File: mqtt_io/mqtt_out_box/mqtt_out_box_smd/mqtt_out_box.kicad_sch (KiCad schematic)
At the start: 59 parts, among them J1 Conn_01x04_Pin, J2 Conn_01x02, K1 FINDER-40.52, K2 FINDER-40.52, K3 FINDER-40.52, K4 FINDER-40.52, K5 FINDER-40.52, K6 FINDER-40.52, Q1 IRLML0030, Q2 IRLML0030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

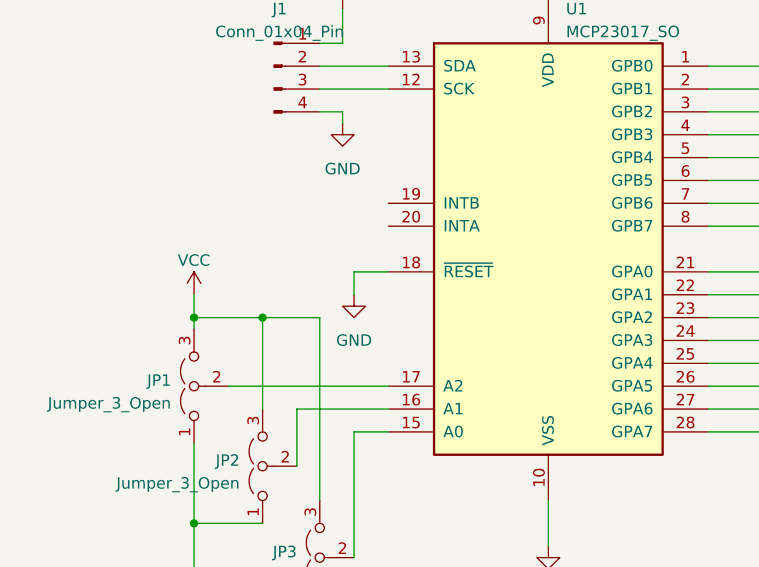
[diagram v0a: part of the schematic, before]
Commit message: neue Dateien eingefügt.
out Platine rev 2, testprogramm für pi pico
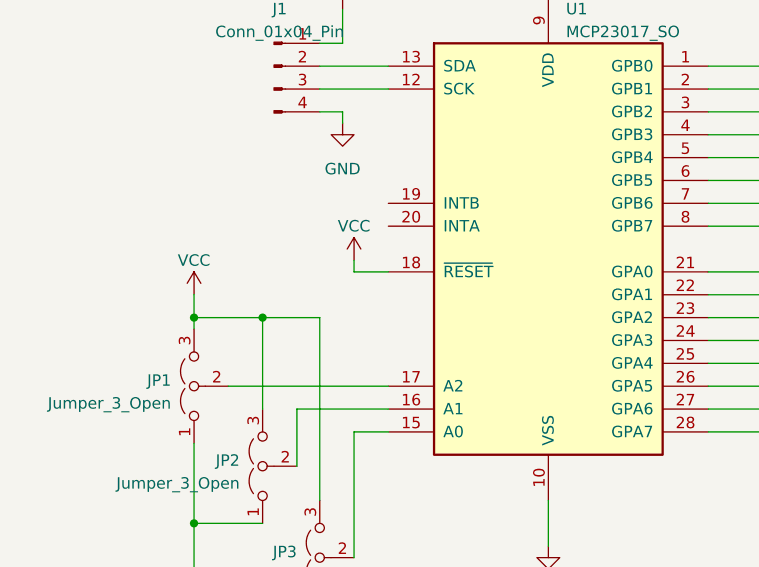
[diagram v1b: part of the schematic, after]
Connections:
- net GND: no longer U1.18 (~{RESET})
- net VCC: now also U1.18 (~{RESET})
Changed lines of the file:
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@@
+    (stroke (width 0) (type default))
+  )
+  (wire (pts (xy 45.72 82.55) (xy 45.72 83.82))
     (stroke (width 0) (type default))
   )
@@
   )
   (wire (pts (xy 264.16 107.95) (xy 264.16 121.92))
-    (stroke (width 0) (type default))
-  )
-  (wire (pts (xy 45.72 83.82) (xy 45.72 86.36))
     (stroke (width 0) (type default))
   )
@@
     )
   )
-  (symbol (lib_id "power:GND") (at 45.72 86.36 0) (unit 1)
-    (in_bom yes) (on_board yes) (dnp no) (fields_autoplaced)
-    (property "Reference" "#PWR05" (at 45.72 92.71 0)
-      (effects (font (size 1.27 1.27)) hide)
-    )
-    (property "Value" "GND" (at 45.72 91.44 0)
-      (effects (font (size 1.27 1.27)))
-    )
-    (property "Footprint" "" (at 45.72 86.36 0)
-      (effects (font (size 1.27 1.27)) hide)
-    )
-    (property "Datasheet" "" (at 45.72 86.36 0)
-      (effects (font (size 1.27 1.27)) hide)
-    )
-    (pin "1")
-    (instances
-      (project "mqtt_out_box"
-        (path "/d6a7dd6e-fa52-4ea7-ba98-8f1dfc1763a3"
-          (reference "#PWR05") (unit 1)
-        )
-      )
-    )
-  )
   (symbol (lib_id "Connector:Conn_01x04_Pin") (at 36.83 60.96 0) (unit 1)
     (in_bom yes) (on_board yes) (dnp no)
@@
         )
       )
+    )
+  )
+  (symbol (lib_id "power:VCC") (at 45.72 82.55 0) (unit 1)
+    (in_bom yes) (on_board yes) (dnp no) (fields_autoplaced)
+    (property "Reference" "#PWR05" (at 45.72 86.36 0)
+      (effects (font (size 1.27 1.27)) hide)
+    )
+    (property "Value" "VCC" (at 45.72 78.74 0)
+      (effects (font (size 1.27 1.27)))
+    )
+    (property "Footprint" "" (at 45.72 82.55 0)
+      (effects (font (size 1.27 1.27)) hide)
+    )
+    (property "Datasheet" "" (at 45.72 82.55 0)
+      (effects (font (size 1.27 1.27)) hide)
+    )
+    (pin "1")
+    (instances
+      (project "mqtt_out_box"
+        (path "/d6a7dd6e-fa52-4ea7-ba98-8f1dfc1763a3"
+          (reference "#PWR05") (unit 1)
+        )
+      )
